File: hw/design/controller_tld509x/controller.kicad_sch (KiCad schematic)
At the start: 54 parts, among them J1 Conn_ARM_SWD_TagConnect_TC203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, J3 Conn_02x01, Q1 PSMN5R2-60YL, Q5 SiSS27DN, Q601 2N7002, U2 TLD509x, U300 MCP2021A-330E/SN, U4 ATSAMC21E18A-MNT

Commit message: Final hardware design
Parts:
- C3: value 47n -> 100n
- C412: value 4.7u -> 10u
- Q1: value PSMN5R2-60YL -> BUK7Y7R0-40HX
- Q5: value SiSS27DN -> BUK6Y24-40PX
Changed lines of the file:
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@@
       (effects (font (size 1.27 1.27)))
     )
-    (property "Value" "47n" (at 186.69 146.685 0)
+    (property "Value" "100n" (at 186.69 146.685 0)
       (effects (font (size 1.27 1.27)))
     )
@@
       (effects (font (size 1.27 1.27)) (justify left))
     )
-    (property "Value" "PSMN5R2-60YL" (at 266.7 85.725 0)
+    (property "Value" "BUK7Y7R0-40HX" (at 266.7 85.725 0)
       (effects (font (size 1.27 1.27)) (justify left))
     )
@@
       (effects (font (size 1.27 1.27)))
     )
-    (property "Value" "SiSS27DN" (at 232.41 55.88 90)
+    (property "Value" "BUK6Y24-40PX" (at 232.41 55.88 90)
       (effects (font (size 1.27 1.27)))
     )
@@
       (effects (font (size 1.27 1.27)))
     )
-    (property "Value" "4.7u" (at 238.125 40.005 90)
-      (effects (font (size 1.27 1.27)))
-    )
+    (property "Value" "10u" (at 238.125 40.005 90)
+      (effects (font (size 1.27 1.27)))
+    )

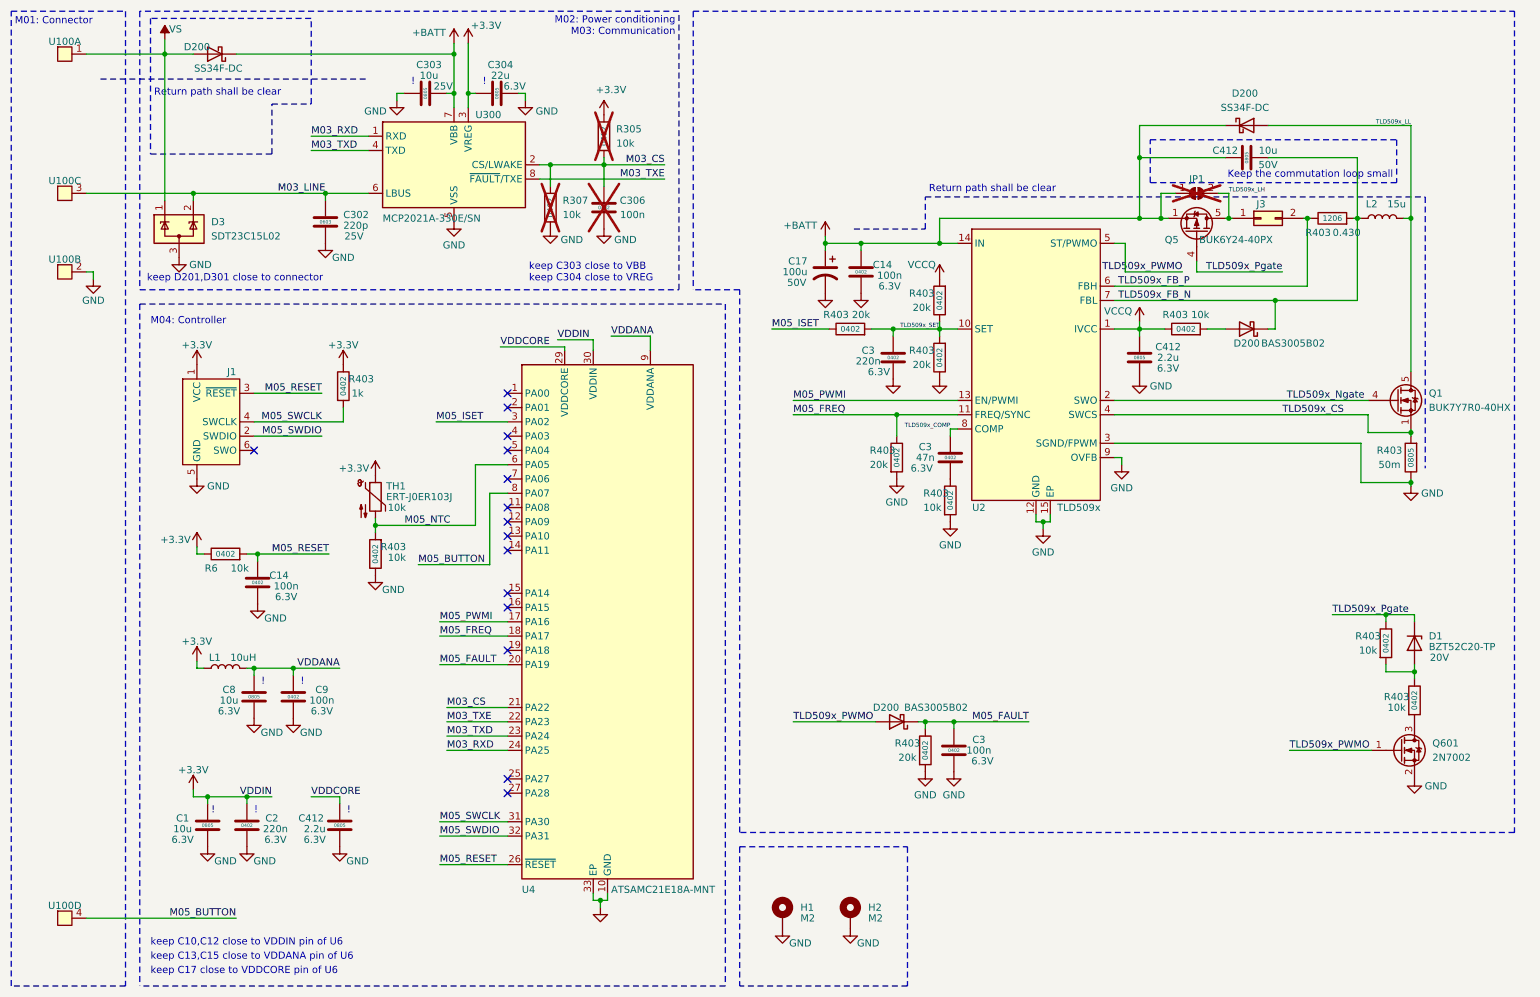
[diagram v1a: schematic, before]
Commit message: Hardware schematic cleanup
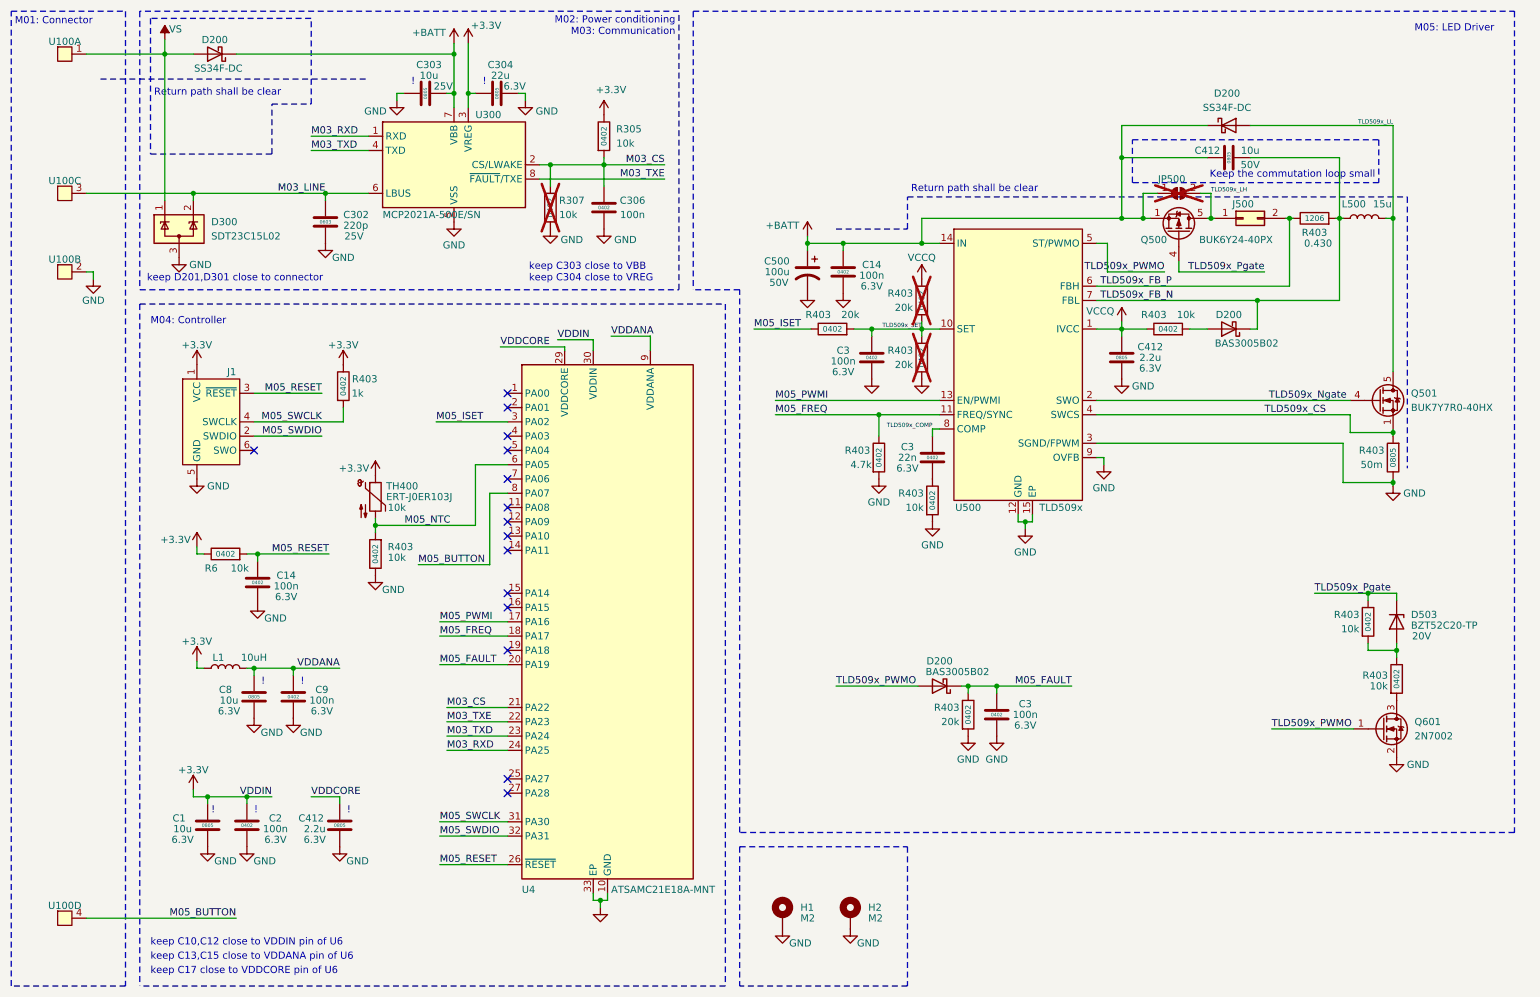
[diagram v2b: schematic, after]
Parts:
- C2, C3: value 220n -> 100n
- C3: value 47n -> 22n
- C306, R305: now fitted
- R403: now not fitted
- R403: value 20k -> 4.7k
- U300: value MCP2021A-330E/SN -> MCP2021A-500E/SN
- renumbered C17 to C500, D3 to D300, D1 to D503, J3 to J500, JP1 to JP500, L2 to L500, Q5 to Q500, Q1 to Q501, TH1 to TH400, U2 to U500
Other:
- note added: "M05: LED Driver"
- moved on the sheet: C14, C3, C412, C500, D200, D503, J500, JP500, L500, Q500, Q501, Q601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
